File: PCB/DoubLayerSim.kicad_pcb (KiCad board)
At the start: 2 copper layers, 92.8 x 74.4 mm, 26 parts, among them J1 PanelSolar, J2 Bateria 3.7v, Q1 2N3904, U1 Moisture

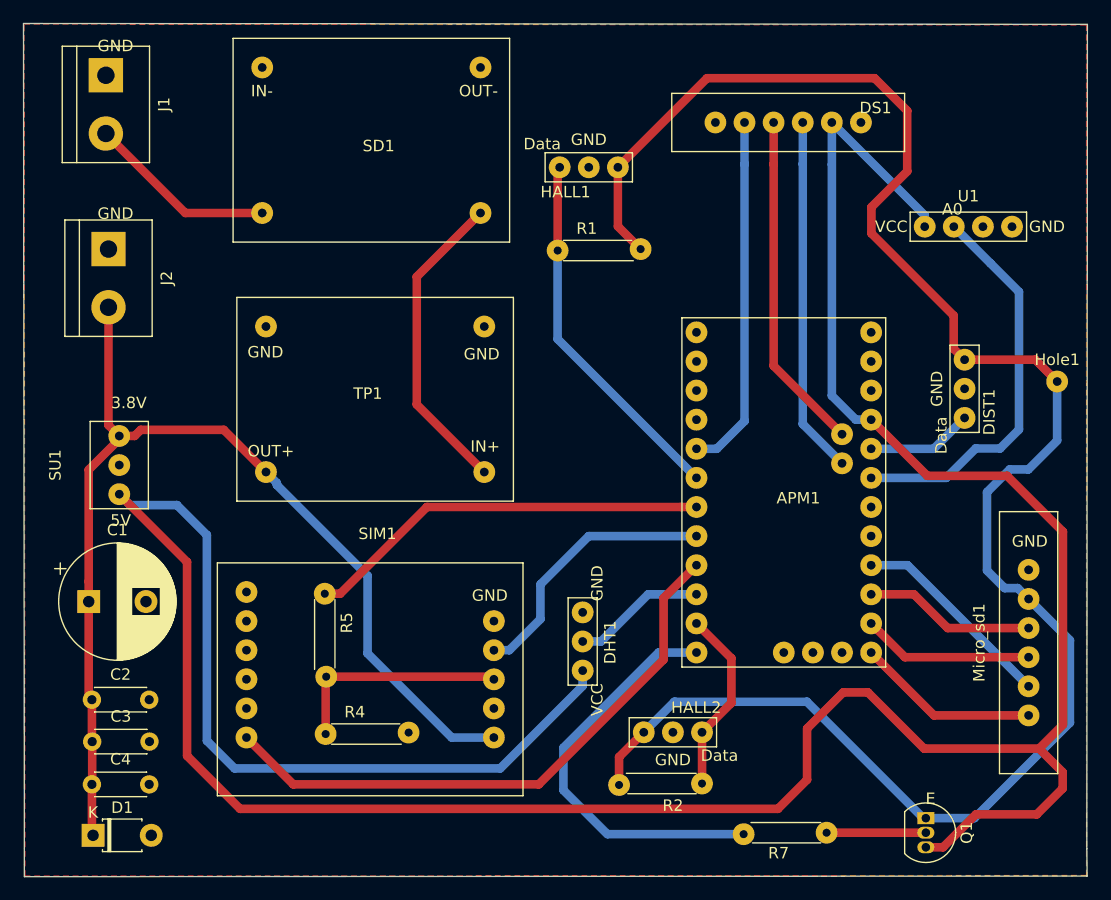
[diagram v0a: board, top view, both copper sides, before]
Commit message: Cambio PCB Devolucion China
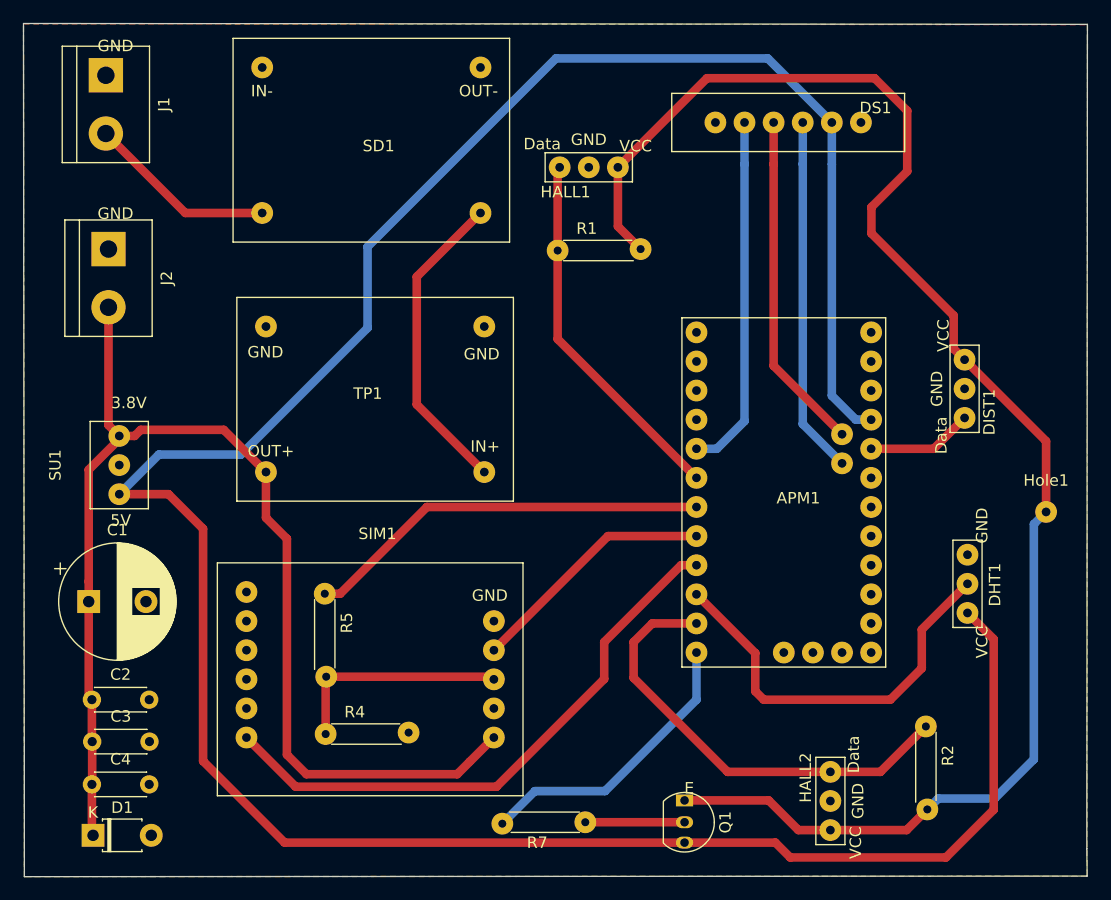
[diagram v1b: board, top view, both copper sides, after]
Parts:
- removed Micro_sd1: MicroSdAdapter, pcb_ss:MicroSD_Adapter
- removed U1: Moisture, pcb_ss:MOIS
- Hole1: footprint MountingHole:MountingHole_2.5mm_Pad -> MountingHole:MountingHole_2.2mm_M2_ISO7380_Pad
- moved DHT1 34.0 mm to (196.6, 94.6)
- moved Q1 21.1 mm to (171.9, 114.2)
- moved R7 21.1 mm to (163.3, 115.4)
- moved R2 20.2 mm to (193.0, 107.1), turned to 270 degrees
- moved HALL2 15.0 mm to (184.7, 113.6), turned to 90 degrees
- moved Hole1 11.3 mm to (203.5, 88.4)
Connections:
- APM1 pad 18: Net-(APM1-Pad18) -> (no net)
- APM1 pad 21: Net-(APM1-Pad21) -> (no net)
- APM1 pad 22: Net-(APM1-Pad22) -> (no net)
- APM1 pad 23: Net-(APM1-Pad23) -> (no net)
- APM1 pad 24: Net-(APM1-Pad24) -> (no net)
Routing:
- net +5V: track 275.2 -> 233.7 mm
- net Net-(APM1-Pad18): track 34.7 -> 0.00 mm
- net VCCQ: track 161.5 -> 136.6 mm
- net Net-(APM1-Pad10): track 11.6 -> 35.6 mm
- net Net-(APM1-Pad11): track 16.3 -> 39.8 mm
- net Net-(APM1-Pad21): track 18.1 -> 0.00 mm
- net Net-(APM1-Pad24): track 16.0 -> 0.00 mm
- net Net-(APM1-Pad23): track 15.0 -> 0.00 mm
- net Net-(APM1-Pad22): track 15.0 -> 0.00 mm
- net +3V8: track 95.9 -> 107.8 mm
- net Net-(APM1-Pad12): track 36.1 -> 25.5 mm
- net Net-(APM1-Pad8): track 23.6 -> 21.8 mm
- net Net-(APM1-Pad9): track 52.0 -> 50.9 mm
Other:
- board text added: "VCC"
